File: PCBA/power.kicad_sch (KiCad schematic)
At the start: 8 parts

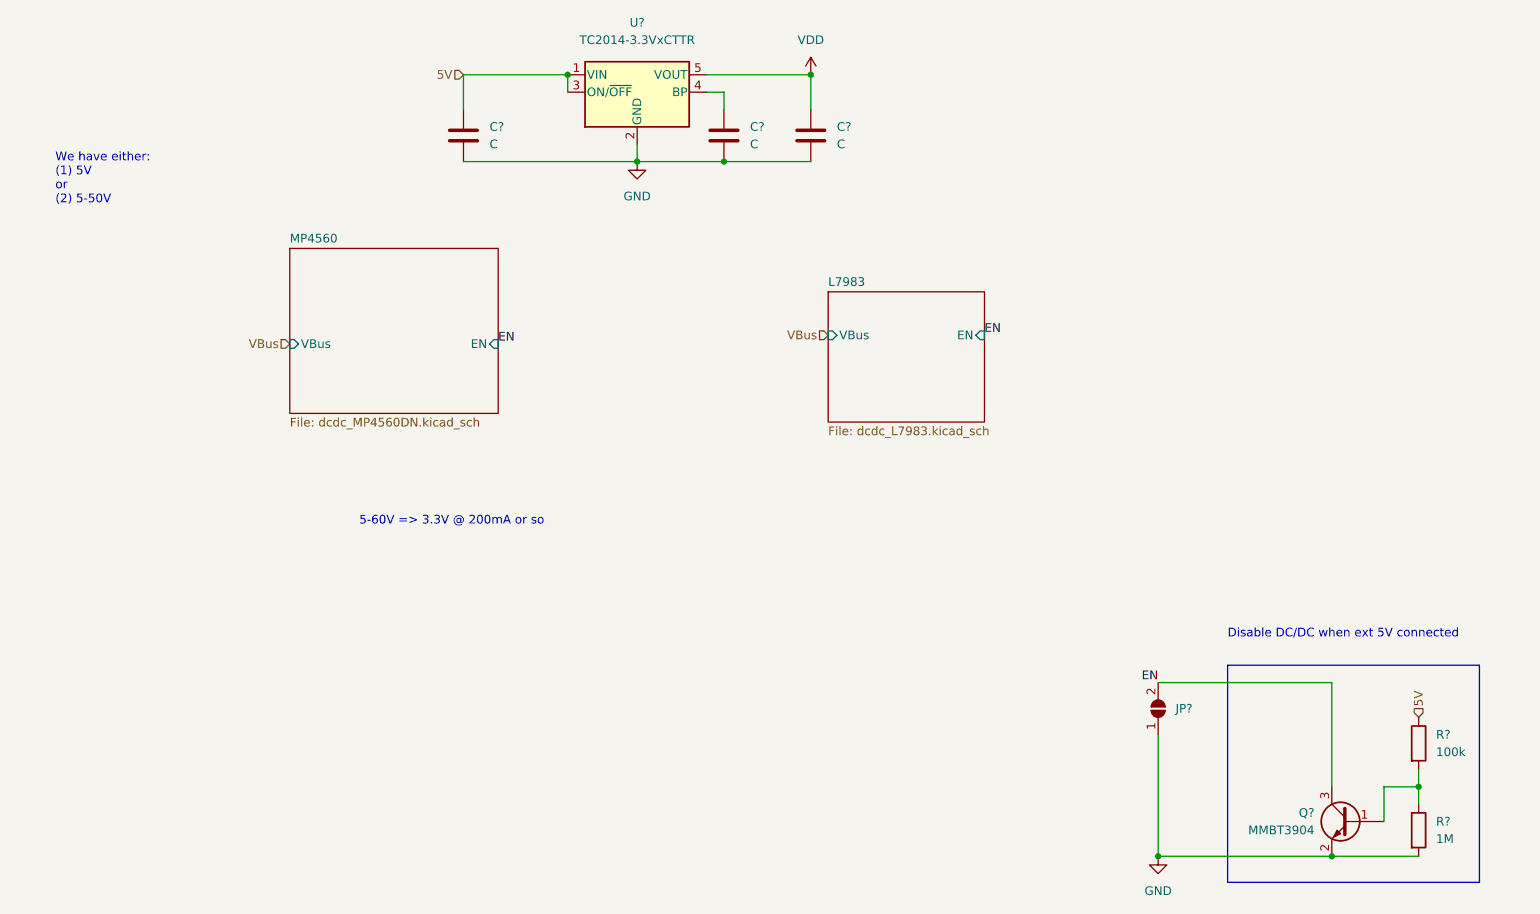
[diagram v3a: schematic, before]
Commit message: Assign footprints
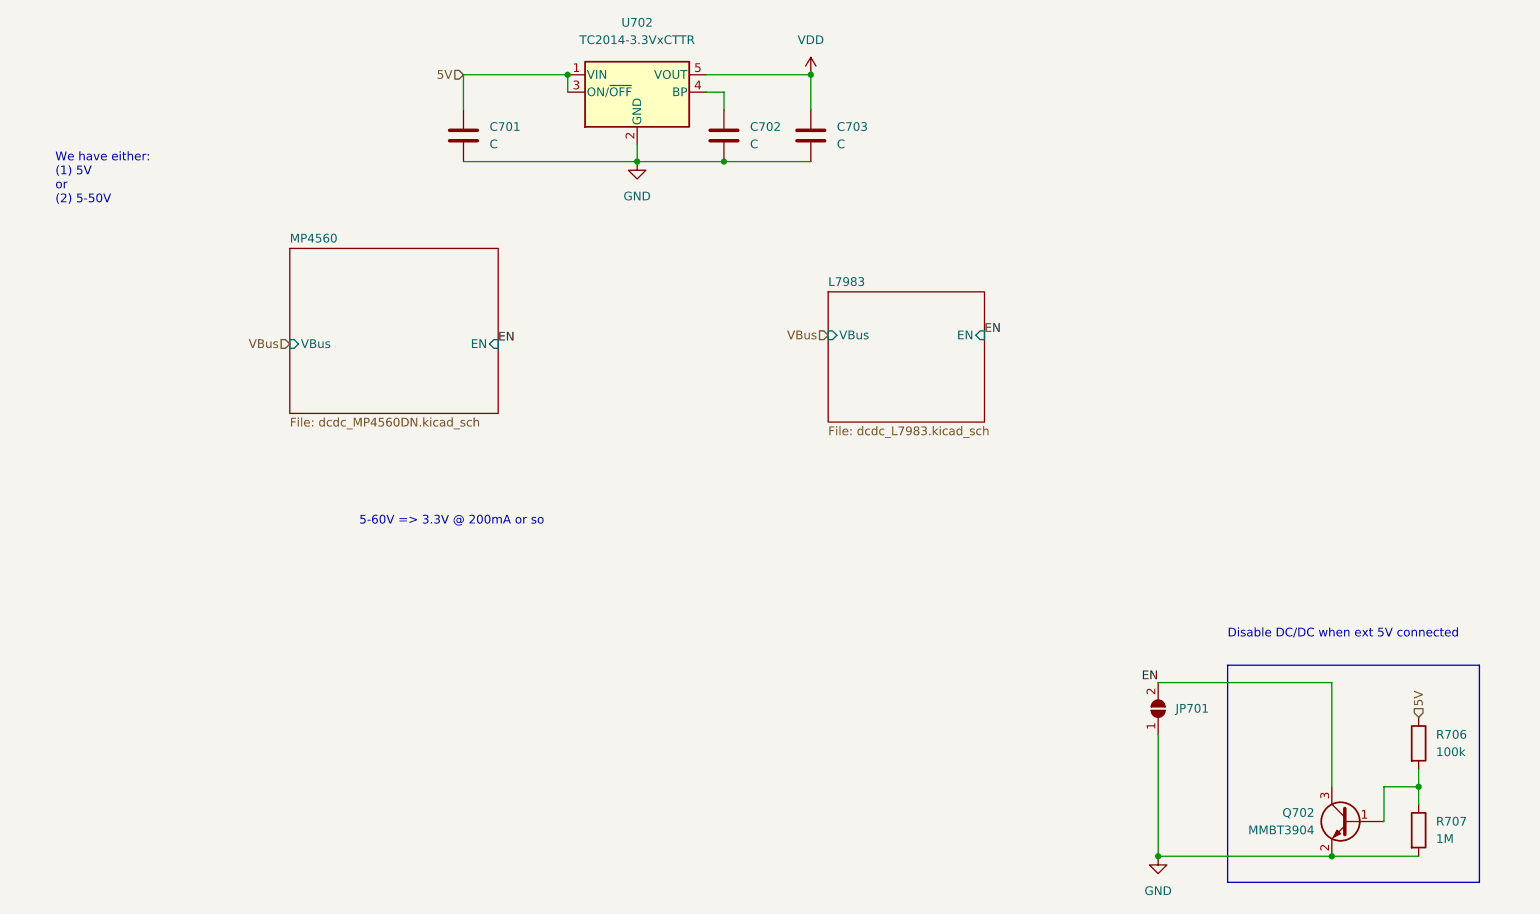
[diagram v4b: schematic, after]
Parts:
- C701, C702, C703: renamed from C?; footprint (none) -> Capacitor_SMD:C_0603_1608Metric
- JP701: renamed from JP?; footprint (none) -> Jumper:SolderJumper-2_P1.3mm_Open_Pad1.0x1.5mm
- R706, R707: renamed from R?; footprint (none) -> Resistor_SMD:R_0603_1608Metric
- gave numbers to parts that had none: 2
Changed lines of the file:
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@@
   (symbol (lib_id "Regulator_Linear:TC2014-3.3VxCTTR") (at 152.4 27.94 0) (unit 1)
     (in_bom yes) (on_board yes) (fields_autoplaced)
-    (property "Reference" "U?" (id 0) (at 152.4 17.78 0))
+    (property "Reference" "U702" (id 0) (at 152.4 17.78 0))
     (property "Value" "TC2014-3.3VxCTTR" (id 1) (at 152.4 20.32 0))
     (property "Footprint" "Package_TO_SOT_SMD:SOT-23-5" (id 2) (at 152.4 19.685 0)
@@
   (symbol (lib_id "Jumper:SolderJumper_2_Open") (at 228.6 118.11 90) (unit 1)
     (in_bom yes) (on_board yes) (fields_autoplaced)
-    (property "Reference" "JP?" (id 0) (at 231.14 118.1099 90)
+    (property "Reference" "JP701" (id 0) (at 231.14 118.1099 90)
       (effects (font (size 1.27 1.27)) (justify right))
     )
@@
       (effects (font (size 1.27 1.27)) (justify right) hide)
     )
-    (property "Footprint" "" (id 2) (at 228.6 118.11 0)
+    (property "Footprint" "Jumper:SolderJumper-2_P1.3mm_Open_Pad1.0x1.5mm" (id 2) (at 228.6 118.11 0)
       (effects (font (size 1.27 1.27)) hide)
     )
@@
   (symbol (lib_id "Device:C") (at 165.1 34.29 0) (unit 1)
     (in_bom yes) (on_board yes) (fields_autoplaced)
-    (property "Reference" "C?" (id 0) (at 168.91 33.0199 0)
+    (property "Reference" "C702" (id 0) (at 168.91 33.0199 0)
       (effects (font (size 1.27 1.27)) (justify left))
     )
@@
       (effects (font (size 1.27 1.27)) (justify left))
     )
-    (property "Footprint" "" (id 2) (at 166.0652 38.1 0)
+    (property "Footprint" "Capacitor_SMD:C_0603_1608Metric" (id 2) (at 166.0652 38.1 0)
       (effects (font (size 1.27 1.27)) hide)
     )
@@
   (symbol (lib_id "Device:R") (at 266.7 123.19 0) (unit 1)
     (in_bom yes) (on_board yes) (fields_autoplaced)
-    (property "Reference" "R?" (id 0) (at 269.24 121.9199 0)
+    (property "Reference" "R706" (id 0) (at 269.24 121.9199 0)
       (effects (font (size 1.27 1.27)) (justify left))
     )
@@
       (effects (font (size 1.27 1.27)) (justify left))
     )
-    (property "Footprint" "" (id 2) (at 264.922 123.19 90)
+    (property "Footprint" "Resistor_SMD:R_0603_1608Metric" (id 2) (at 264.922 123.19 90)
       (effects (font (size 1.27 1.27)) hide)
     )
@@
   (symbol (lib_id "Device:R") (at 266.7 135.89 0) (unit 1)
     (in_bom yes) (on_board yes) (fields_autoplaced)
-    (property "Reference" "R?" (id 0) (at 269.24 134.6199 0)
+    (property "Reference" "R707" (id 0) (at 269.24 134.6199 0)
       (effects (font (size 1.27 1.27)) (justify left))
     )
@@
       (effects (font (size 1.27 1.27)) (justify left))
     )
-    (property "Footprint" "" (id 2) (at 264.922 135.89 90)
+    (property "Footprint" "Resistor_SMD:R_0603_1608Metric" (id 2) (at 264.922 135.89 90)
       (effects (font (size 1.27 1.27)) hide)
     )
@@
   (symbol (lib_id "Device:C") (at 177.8 34.29 0) (unit 1)
     (in_bom yes) (on_board yes) (fields_autoplaced)
-    (property "Reference" "C?" (id 0) (at 181.61 33.0199 0)
+    (property "Reference" "C703" (id 0) (at 181.61 33.0199 0)
       (effects (font (size 1.27 1.27)) (justify left))
     )
@@
       (effects (font (size 1.27 1.27)) (justify left))
     )
-    (property "Footprint" "" (id 2) (at 178.7652 38.1 0)
+    (property "Footprint" "Capacitor_SMD:C_0603_1608Metric" (id 2) (at 178.7652 38.1 0)
       (effects (font (size 1.27 1.27)) hide)
     )
@@
   (symbol (lib_id "power:GND") (at 228.6 139.7 0) (unit 1)
     (in_bom yes) (on_board yes) (fields_autoplaced)
-    (property "Reference" "#PWR?" (id 0) (at 228.6 146.05 0)
+    (property "Reference" "#PWR0154" (id 0) (at 228.6 146.05 0)
       (effects (font (size 1.27 1.27)) hide)
     )
@@
   (symbol (lib_id "Device:C") (at 127 34.29 0) (unit 1)
     (in_bom yes) (on_board yes) (fields_autoplaced)
-    (property "Reference" "C?" (id 0) (at 130.81 33.0199 0)
+    (property "Reference" "C701" (id 0) (at 130.81 33.0199 0)
       (effects (font (size 1.27 1.27)) (justify left))
     )
@@
       (effects (font (size 1.27 1.27)) (justify left))
     )
-    (property "Footprint" "" (id 2) (at 127.9652 38.1 0)
+    (property "Footprint" "Capacitor_SMD:C_0603_1608Metric" (id 2) (at 127.9652 38.1 0)
       (effects (font (size 1.27 1.27)) hide)
     )
@@
   (symbol (lib_id "Transistor_BJT:MMBT3904") (at 256.54 134.62 0) (mirror y) (unit 1)
     (in_bom yes) (on_board yes) (fields_autoplaced)
-    (property "Reference" "Q?" (id 0) (at 251.46 133.3499 0)
+    (property "Reference" "Q702" (id 0) (at 251.46 133.3499 0)
       (effects (font (size 1.27 1.27)) (justify left))
     )
@@
   (symbol (lib_id "power:VDD") (at 177.8 25.4 0) (unit 1)
     (in_bom yes) (on_board yes) (fields_autoplaced)
-    (property "Reference" "#PWR?" (id 0) (at 177.8 29.21 0)
+    (property "Reference" "#PWR0153" (id 0) (at 177.8 29.21 0)
       (effects (font (size 1.27 1.27)) hide)
     )
@@
   (symbol (lib_id "power:GND") (at 152.4 38.1 0) (unit 1)
     (in_bom yes) (on_board yes) (fields_autoplaced)
-    (property "Reference" "#PWR?" (id 0) (at 152.4 44.45 0)
+    (property "Reference" "#PWR0152" (id 0) (at 152.4 44.45 0)
       (effects (font (size 1.27 1.27)) hide)
     )

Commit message: Rough outline
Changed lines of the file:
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@@
+    (stroke (width 0) (type default) (color 0 0 0 0))
+  )
+  (polyline (pts (xy 114.3 78.74) (xy 114.3 88.9))
     (stroke (width 0) (type default) (color 0 0 0 0))
   )
   (polyline (pts (xy 275.59 143.51) (xy 275.59 111.76))
+    (stroke (width 0) (type default) (color 0 0 0 0))
+  )
+  (polyline (pts (xy 190.5 81.28) (xy 190.5 88.9))
     (stroke (width 0) (type default) (color 0 0 0 0))
   )
@@
   )
   (polyline (pts (xy 238.76 143.51) (xy 275.59 143.51))
+    (stroke (width 0) (type default) (color 0 0 0 0))
+  )
+  (polyline (pts (xy 176.53 88.9) (xy 190.5 88.9))
+    (stroke (width 0) (type default) (color 0 0 0 0))
+  )
+  (polyline (pts (xy 140.97 88.9) (xy 114.3 88.9))
     (stroke (width 0) (type default) (color 0 0 0 0))
   )
@@
     (effects (font (size 1.27 1.27)) (justify left bottom))
   )
-  (text "5-60V => 3.3V @ 200mA or so" (at 111.76 91.44 0)
+  (text "5-60V => 3.3V @ 200mA or so" (at 143.51 90.17 0)
     (effects (font (size 1.27 1.27)) (justify left bottom))
   )
